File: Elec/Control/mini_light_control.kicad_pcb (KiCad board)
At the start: 2 copper layers, 63 x 28 mm, 40 parts, among them J1 Conn_01x04, J2 Conn_01x02, J3 Conn_01x02, J4 Conn_01x03, J5 Conn_01x03, J6 Conn_01x02, J7 Conn_01x02, J8 Conn_01x03, J9 Conn_01x03, U1 LM2904DT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

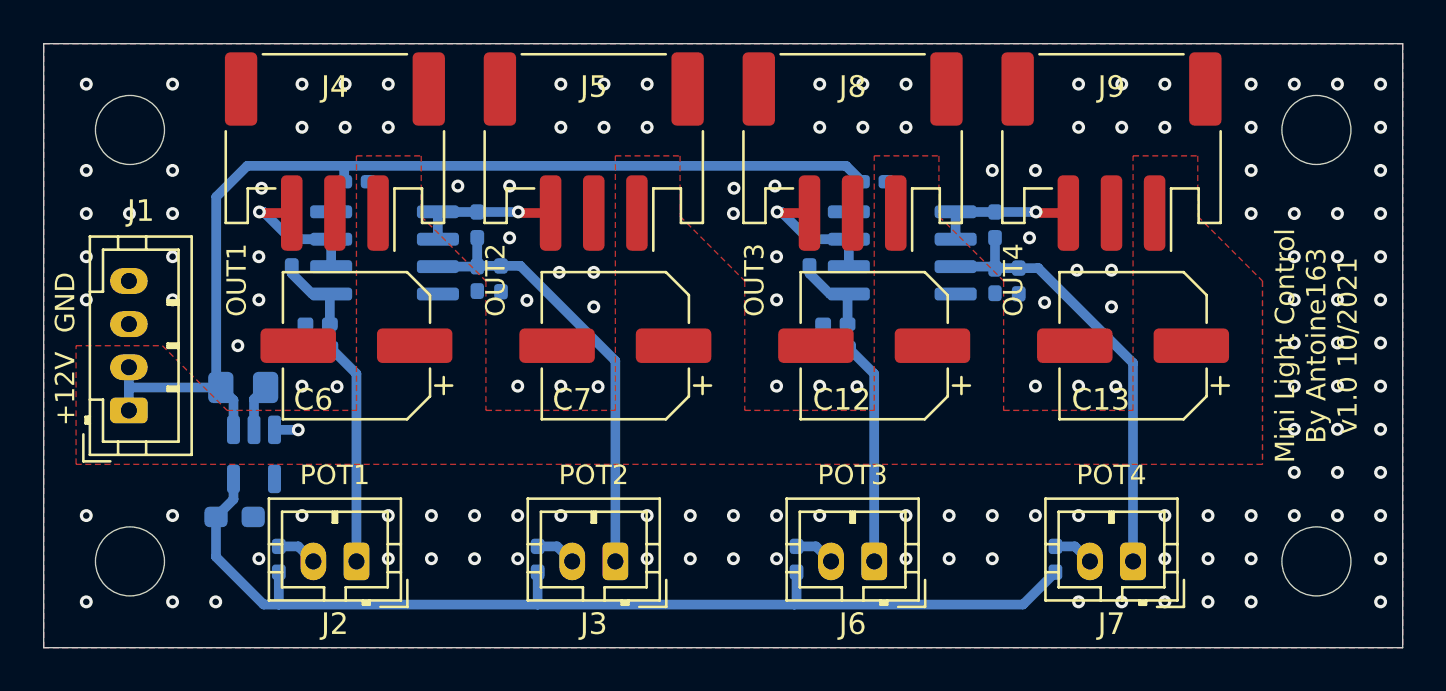
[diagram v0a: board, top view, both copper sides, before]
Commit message: Add protection diode for LDO and change power connector.
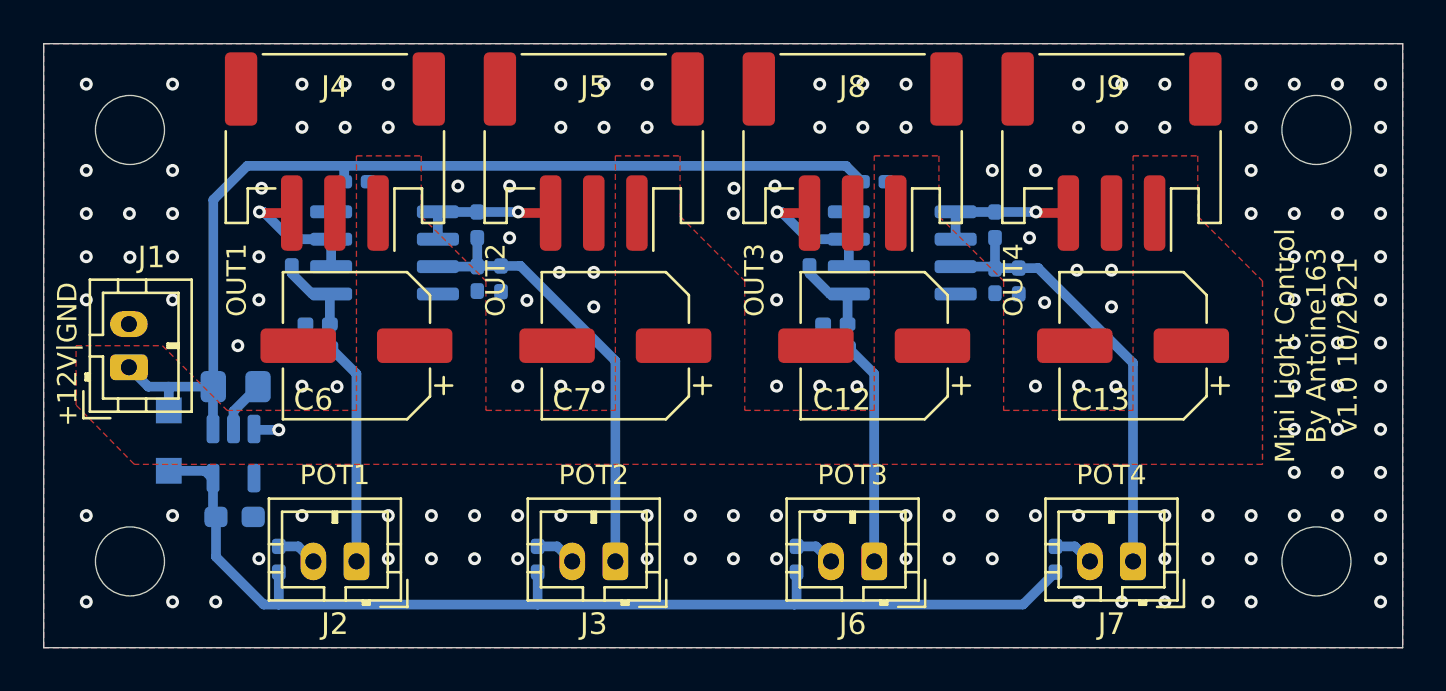
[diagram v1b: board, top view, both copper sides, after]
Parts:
- added D1: PMEG40T10ERX, Diode_SMD:Nexperia_CFP3_SOD-123W, B.Cu at (106.3, 53.4)
- J1: value Conn_01x04 -> Conn_01x02; footprint Connector_JST:JST_PH_B4B-PH-K_1x04_P2.00mm_Vertical -> Connector_JST:JST_PH_B2B-PH-K_1x02_P2.00mm_Vertical
- moved J1 2.00 mm to (104.5, 50.0)
- moved U2 0.95 mm to (109.3, 54.0)
- moved C5 0.35 mm to (109.4, 50.9)
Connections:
- J1 pad 2: +12V -> GND
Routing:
- net +5V: track 48.9 -> 50.9 mm
- net +12V: track 53.4 -> 52.2 mm
- net GND: track 2.19 -> 2.47 mm, vias 148 -> 149
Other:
- board text added: "+12V|GND"
- board text removed: "+12V"
- board text removed: "GND"

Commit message: Change simbol connector to 'MountingPin' version
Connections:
- J4 pad MP: (no net) -> GND
- J5 pad MP: (no net) -> GND
- J8 pad MP: (no net) -> GND
- J9 pad MP: (no net) -> GND
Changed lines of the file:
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@@
     (pad "3" smd roundrect locked (at 2 -2.85 180) (size 1 3.5) (layers "F.Cu" "F.Paste" "F.Mask") (roundrect_rratio 0.25)
       (net 9 "Net-(J4-Pad3)") (pinfunction "Pin_3") (pintype "passive"))
-    (pad "MP" smd roundrect locked (at 4.35 2.9 180) (size 1.5 3.4) (layers "F.Cu" "F.Paste" "F.Mask") (roundrect_rratio 0.1666673333))
-    (pad "MP" smd roundrect locked (at -4.35 2.9 180) (size 1.5 3.4) (layers "F.Cu" "F.Paste" "F.Mask") (roundrect_rratio 0.1666673333))
+    (pad "MP" smd roundrect locked (at 4.35 2.9 180) (size 1.5 3.4) (layers "F.Cu" "F.Paste" "F.Mask") (roundrect_rratio 0.1666673333)
+      (net 1 "GND") (pinfunction "MountPin") (pintype "passive"))
+    (pad "MP" smd roundrect locked (at -4.35 2.9 180) (size 1.5 3.4) (layers "F.Cu" "F.Paste" "F.Mask") (roundrect_rratio 0.1666673333)
+      (net 1 "GND") (pinfunction "MountPin") (pintype "passive"))
     (model "${KICAD6_3DMODEL_DIR}/Connector_JST.3dshapes/JST_PH_S3B-PH-SM4-TB_1x03-1MP_P2.00mm_Horizontal.wrl"
       (offset (xyz 0 0 0))
@@
     (pad "3" smd roundrect locked (at 2 -2.85 180) (size 1 3.5) (layers "F.Cu" "F.Paste" "F.Mask") (roundrect_rratio 0.25)
       (net 13 "Net-(J8-Pad3)") (pinfunction "Pin_3") (pintype "passive"))
-    (pad "MP" smd roundrect locked (at 4.35 2.9 180) (size 1.5 3.4) (layers "F.Cu" "F.Paste" "F.Mask") (roundrect_rratio 0.1666673333))
-    (pad "MP" smd roundrect locked (at -4.35 2.9 180) (size 1.5 3.4) (layers "F.Cu" "F.Paste" "F.Mask") (roundrect_rratio 0.1666673333))
+    (pad "MP" smd roundrect locked (at 4.35 2.9 180) (size 1.5 3.4) (layers "F.Cu" "F.Paste" "F.Mask") (roundrect_rratio 0.1666673333)
+      (net 1 "GND") (pinfunction "MountPin") (pintype "passive"))
+    (pad "MP" smd roundrect locked (at -4.35 2.9 180) (size 1.5 3.4) (layers "F.Cu" "F.Paste" "F.Mask") (roundrect_rratio 0.1666673333)
+      (net 1 "GND") (pinfunction "MountPin") (pintype "passive"))
     (model "${KICAD6_3DMODEL_DIR}/Connector_JST.3dshapes/JST_PH_S3B-PH-SM4-TB_1x03-1MP_P2.00mm_Horizontal.wrl"
       (offset (xyz 0 0 0))
@@
     (pad "3" smd roundrect locked (at 2 -2.85 180) (size 1 3.5) (layers "F.Cu" "F.Paste" "F.Mask") (roundrect_rratio 0.25)
       (net 14 "Net-(J9-Pad3)") (pinfunction "Pin_3") (pintype "passive"))
-    (pad "MP" smd roundrect locked (at -4.35 2.9 180) (size 1.5 3.4) (layers "F.Cu" "F.Paste" "F.Mask") (roundrect_rratio 0.1666673333))
-    (pad "MP" smd roundrect locked (at 4.35 2.9 180) (size 1.5 3.4) (layers "F.Cu" "F.Paste" "F.Mask") (roundrect_rratio 0.1666673333))
+    (pad "MP" smd roundrect locked (at -4.35 2.9 180) (size 1.5 3.4) (layers "F.Cu" "F.Paste" "F.Mask") (roundrect_rratio 0.1666673333)
+      (net 1 "GND") (pinfunction "MountPin") (pintype "passive"))
+    (pad "MP" smd roundrect locked (at 4.35 2.9 180) (size 1.5 3.4) (layers "F.Cu" "F.Paste" "F.Mask") (roundrect_rratio 0.1666673333)
+      (net 1 "GND") (pinfunction "MountPin") (pintype "passive"))
     (model "${KICAD6_3DMODEL_DIR}/Connector_JST.3dshapes/JST_PH_S3B-PH-SM4-TB_1x03-1MP_P2.00mm_Horizontal.wrl"
       (offset (xyz 0 0 0))
@@
     (pad "3" smd roundrect locked (at 2 -2.85 180) (size 1 3.5) (layers "F.Cu" "F.Paste" "F.Mask") (roundrect_rratio 0.25)
       (net 10 "Net-(J5-Pad3)") (pinfunction "Pin_3") (pintype "passive"))
-    (pad "MP" smd roundrect locked (at -4.35 2.9 180) (size 1.5 3.4) (layers "F.Cu" "F.Paste" "F.Mask") (roundrect_rratio 0.1666673333))
-    (pad "MP" smd roundrect locked (at 4.35 2.9 180) (size 1.5 3.4) (layers "F.Cu" "F.Paste" "F.Mask") (roundrect_rratio 0.1666673333))
+    (pad "MP" smd roundrect locked (at -4.35 2.9 180) (size 1.5 3.4) (layers "F.Cu" "F.Paste" "F.Mask") (roundrect_rratio 0.1666673333)
+      (net 1 "GND") (pinfunction "MountPin") (pintype "passive"))
+    (pad "MP" smd roundrect locked (at 4.35 2.9 180) (size 1.5 3.4) (layers "F.Cu" "F.Paste" "F.Mask") (roundrect_rratio 0.1666673333)
+      (net 1 "GND") (pinfunction "MountPin") (pintype "passive"))
     (model "${KICAD6_3DMODEL_DIR}/Connector_JST.3dshapes/JST_PH_S3B-PH-SM4-TB_1x03-1MP_P2.00mm_Horizontal.wrl"
       (offset (xyz 0 0 0))
@@
     (fp_line (start -0.8 0.4) (end 0.8 0.4) (layer "B.Fab") (width 0.1))
     (pad "1" smd roundrect locked (at -0.8625 0) (size 1.075 0.95) (layers "B.Cu" "B.Paste" "B.Mask") (roundrect_rratio 0.25)
-      (net 15 "+5V"))
+      (net 15 "+5V") (pintype "passive"))
     (pad "2" smd roundrect locked (at 0.8625 0) (size 1.075 0.95) (layers "B.Cu" "B.Paste" "B.Mask") (roundrect_rratio 0.25)
-      (net 1 "GND"))
+      (net 1 "GND") (pintype "passive"))
     (model "${KICAD6_3DMODEL_DIR}/Capacitor_SMD.3dshapes/C_0603_1608Metric.wrl"
       (offset (xyz 0 0 0))
@@
     (fp_line (start -0.4 1.45) (end 0.8 1.45) (layer "B.Fab") (width 0.1))
     (pad "1" smd roundrect locked (at -1.1375 0.95 270) (size 1.325 0.6) (layers "B.Cu" "B.Paste" "B.Mask") (roundrect_rratio 0.25)
-      (net 6 "+12V") (pinfunction "IN"))
+      (net 6 "+12V") (pinfunction "IN") (pintype "power_in"))
     (pad "2" smd roundrect locked (at -1.1375 0 270) (size 1.325 0.6) (layers "B.Cu" "B.Paste" "B.Mask") (roundrect_rratio 0.25)
-      (net 1 "GND") (pinfunction "GND"))
+      (net 1 "GND") (pinfunction "GND") (pintype "power_in"))
     (pad "3" smd roundrect locked (at -1.1375 -0.95 270) (size 1.325 0.6) (layers "B.Cu" "B.Paste" "B.Mask") (roundrect_rratio 0.25)
-      (net 6 "+12V") (pinfunction "EN"))
+      (net 6 "+12V") (pinfunction "EN") (pintype "input"))
     (pad "4" smd roundrect locked (at 1.1375 -0.95 270) (size 1.325 0.6) (layers "B.Cu" "B.Paste" "B.Mask") (roundrect_rratio 0.25)
-      (net 1 "GND") (pinfunction "NC") (thermal_gap 0.2))
+      (net 1 "GND") (pinfunction "NC") (pintype "free") (thermal_gap 0.2))
     (pad "5" smd roundrect locked (at 1.1375 0.95 270) (size 1.325 0.6) (layers "B.Cu" "B.Paste" "B.Mask") (roundrect_rratio 0.25)
-      (net 15 "+5V") (pinfunction "OUT"))
+      (net 15 "+5V") (pinfunction "OUT") (pintype "power_out"))
     (model "${KICAD6_3DMODEL_DIR}/Package_TO_SOT_SMD.3dshapes/SOT-23-5.wrl"
       (offset (xyz 0 0 0))

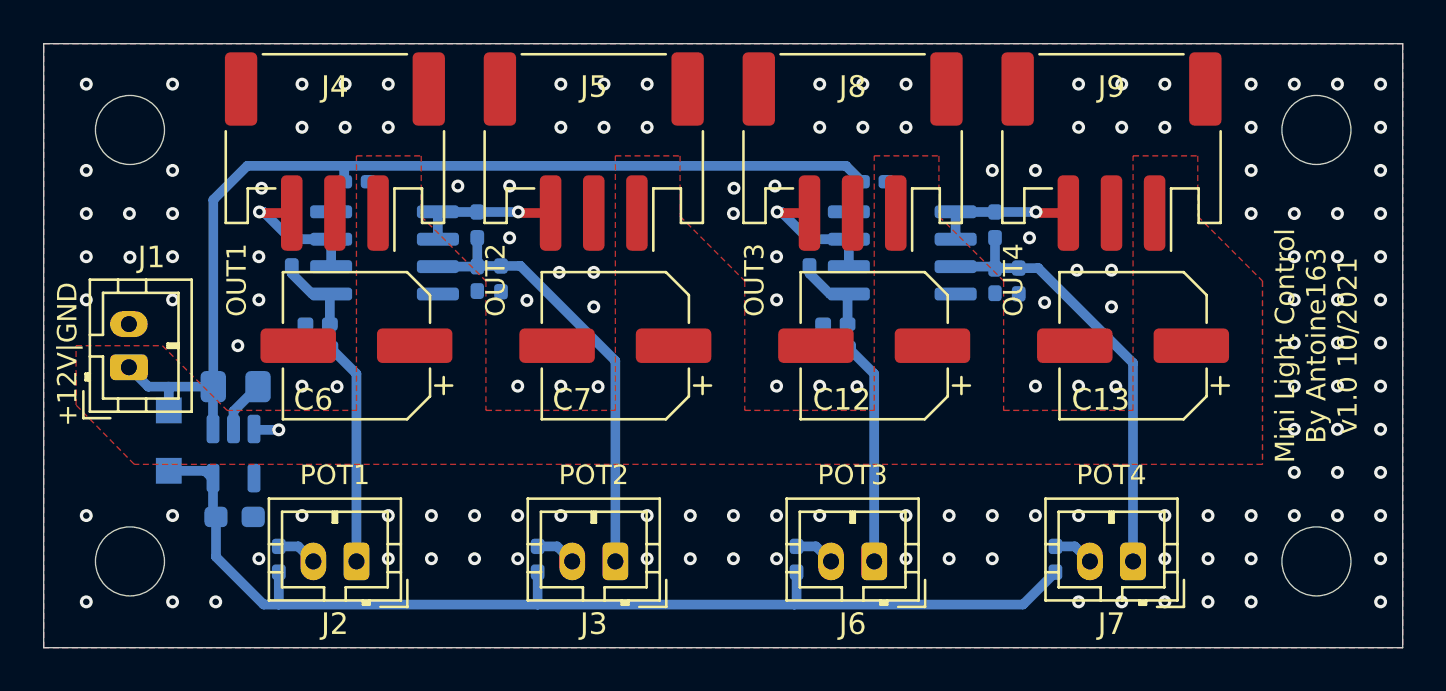
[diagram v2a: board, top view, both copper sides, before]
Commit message: Change JST connector polarity + regenerate gerber file
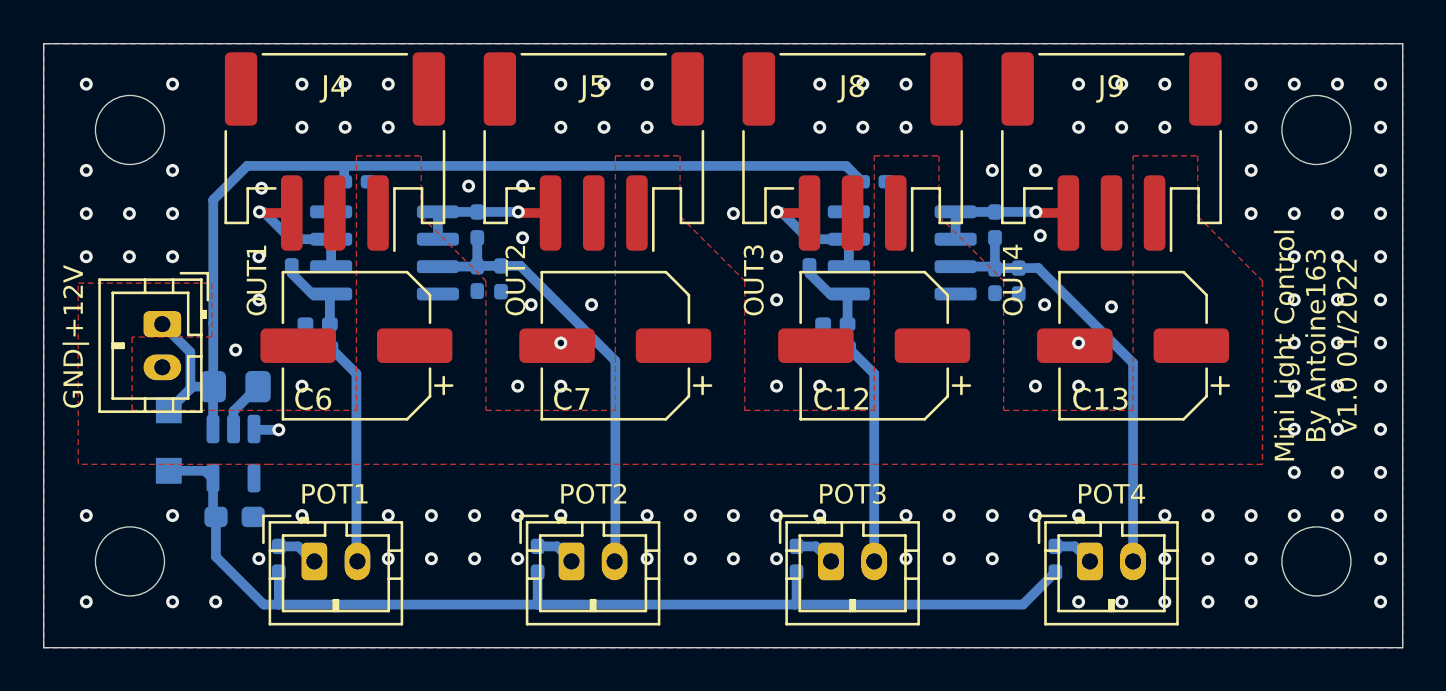
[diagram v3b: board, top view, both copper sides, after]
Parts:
- moved J1 2.53 mm to (106.0, 48.0), turned to -90 degrees
- moved J3 2.03 mm to (125.0, 59.0), turned to 0 degrees
- moved J6 2.00 mm to (137.0, 59.0), turned to 0 degrees
- moved J7 2.00 mm to (149.0, 59.0), turned to 0 degrees
- moved J2 1.95 mm to (113.0, 59.0), turned to 0 degrees
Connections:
- J2 pad 1: Net-(C2-Pad1) -> Net-(R1-Pad1)
- J2 pad 2: Net-(J2-Pad2) -> Net-(C2-Pad1)
- J3 pad 1: Net-(C3-Pad1) -> Net-(R3-Pad1)
- J3 pad 2: Net-(J3-Pad2) -> Net-(C3-Pad1)
- J6 pad 1: Net-(C9-Pad1) -> Net-(R7-Pad1)
- J6 pad 2: Net-(J6-Pad2) -> Net-(C9-Pad1)
- J7 pad 1: Net-(C10-Pad1) -> Net-(R9-Pad1)
- J7 pad 2: Net-(J7-Pad2) -> Net-(C10-Pad1)
- R1 pad 1: Net-(J2-Pad2) -> Net-(R1-Pad1)
- R3 pad 1: Net-(J3-Pad2) -> Net-(R3-Pad1)
- R7 pad 1: Net-(J6-Pad2) -> Net-(R7-Pad1)
- R9 pad 1: Net-(J7-Pad2) -> Net-(R9-Pad1)
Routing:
- net Net-(R9-Pad1): track 0.00 -> 1.89 mm
- net Net-(R7-Pad1): track 0.00 -> 1.89 mm
- net Net-(J7-Pad2): track 1.89 -> 0.00 mm
- net Net-(J6-Pad2): track 1.89 -> 0.00 mm
- net Net-(R3-Pad1): track 0.00 -> 1.89 mm
- net Net-(R1-Pad1): track 0.00 -> 1.89 mm
- net Net-(J3-Pad2): track 1.89 -> 0.00 mm
- net Net-(J2-Pad2): track 1.89 -> 0.00 mm
- net +12V: track 52.2 -> 52.9 mm
- net GND: vias 149 -> 139
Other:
- board text added: "GND|+12V"
- board text added: "Mini Light Control By Antoine163 v1.0 01/2022"
- board text removed: "+12V|GND"
- board text removed: "Mini Light Control By Antoine163 v1.0 10/2021"
